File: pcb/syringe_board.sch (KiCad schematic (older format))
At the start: 33 parts, among them J1 PJ-037A, J2 0855025008, J3 OSTVN08A150, J4 10118194-0001LF, U1 TMC2130, U2 ROF-78E3.3-0.5SMD-R, U3 ATMEGA32U4, X1 feather_wing, Y1 8MHz

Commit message: pcb v3.1
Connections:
- net A2 is gone; now on net CS: U3.38 (PF5(ADC5)), X1.7 (A2)
- net A3 is gone; now on net LIMIT1: U3.39 (PF4(ADC4)), X1.8 (A3)
- net 12VDC: now also C3.1; no longer C3.2
- net 3.3VDC: now also R5.1, R6.1
- net CS: no longer U3.8 (PB0(SS))
- net GND: now also C3.2, U1.2 (CLK); no longer C3.1, R5.1, R6.1
- net LIMIT1: no longer U3.37 (PF6(ADC6)), X1.6 (A1)
- net SCL: now also R6.2, X1.18 (SCL)
- net SDA: now also R5.2, X1.17 (SDA)
- new net A1: U3.37 (PF6(ADC6)), X1.6 (A1)
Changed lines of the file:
@@
 Sheet 1 1
 Title "Syringe Board"
-Date "2019-06-12"
-Rev "3.0"
+Date "2019-06-19"
+Rev "3.1"
 Comp "Andy Lustig"
 Comment1 ""
@@
 $EndComp
 Wire Wire Line
-	3300 2000 3100 2000
-Wire Wire Line
 	2700 1800 2700 1700
-Wire Wire Line
-	2700 1700 3100 1700
 Text Label 3400 1700 2    50   ~ 0
 GND
@@
 Wire Wire Line
 	7400 5700 7300 5700
-Text Label 7400 5650 0    50   ~ 0
-GND
 $Comp
 L Device:LED D1
@@
 Text Label 7600 2500 2    50   ~ 0
 MTR_ENABLE
-Text Label 7600 2600 2    50   ~ 0
-LIMIT1
-Text Label 7600 2700 2    50   ~ 0
-A2
-Text Label 7600 2800 2    50   ~ 0
-A3
 $Comp
 L asl_symbols:feather_wing X1
@@
 Wire Wire Line
 	5550 5400 5450 5400
-Text Label 5450 4300 2    50   ~ 0
-A2
-Text Label 5450 4400 2    50   ~ 0
-A3
 Wire Wire Line
 	7600 3400 7700 3400
@@
 Text Label 5450 4100 2    50   ~ 0
 MTR_ENABLE
-Text Label 5450 4200 2    50   ~ 0
-LIMIT1
 Wire Wire Line
 	7700 3900 7650 3900
@@
 GND
 Wire Wire Line
-	7700 4800 7600 4800
-Text Label 7600 4800 2    50   ~ 0
-CS
-Wire Wire Line
 	1950 4100 1850 4100
 Text Label 1850 4100 2    50   ~ 0
@@
 F 3 "~" H 3100 1850 50  0001 C CNN
 	1    3100 1850
-	1    0    0    -1
-$EndComp
-Wire Wire Line
-	3100 1750 3100 1700
-Connection ~ 3100 1700
-Wire Wire Line
-	3100 1700 3700 1700
-Wire Wire Line
-	3100 1950 3100 2000
-Connection ~ 3100 2000
-Wire Wire Line
-	3100 2000 2700 2000
+	1    0    0    1
+$EndComp
 Text Label 9200 3800 2    50   ~ 0
 D+
@@
 	1    0    0    -1
 $EndComp
+Wire Wire Line
+	2700 1700 3100 1700
+Wire Wire Line
+	2700 2000 3100 2000
+Wire Wire Line
+	3100 1750 3100 1700
+Connection ~ 3100 1700
+Wire Wire Line
+	3100 1700 3700 1700
+Wire Wire Line
+	3100 1950 3100 2000
+Connection ~ 3100 2000
+Wire Wire Line
+	3100 2000 3300 2000
+Text Label 7400 5650 0    50   ~ 0
+3.3VDC
+Text Label 6950 5600 0    50   ~ 0
+SDA
+Text Label 6950 5700 0    50   ~ 0
+SCL
+Wire Wire Line
+	1950 4000 1850 4000
+Text Label 1850 4000 2    50   ~ 0
+GND
+Text Label 7600 2800 2    50   ~ 0
+LIMIT1
+Text Label 7600 2700 2    50   ~ 0
+CS
+Text Label 7600 2600 2    50   ~ 0
+A1
+Text Label 5450 4400 2    50   ~ 0
+LIMIT1
+Text Label 5450 4300 2    50   ~ 0
+CS
+Text Label 5450 4200 2    50   ~ 0
+A1
 $EndSCHEMATC

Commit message: pcb rev 3.2
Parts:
- removed C8: 470nF, Capacitor_SMD:C_0603_1608Metric, symbol Device:C_Small
- removed R3: 2.2Ω, Resistor_SMD:R_0603_1608Metric, symbol Device:R_Small_US
- removed U1: TMC2130, Package_QFP:TQFP-48-1EP_7x7mm_P0.5mm_EP5x5mm_ThermalVias, symbol asl_symbols:TMC2130
- added U1: TMC2208, Package_DFN_QFN:QFN-28-1EP_5x5mm_P0.5mm_EP3.35x3.35mm_ThermalVias, symbol asl_symbols:TMC2208
- C6: renamed from C7; value 4.7uF -> 2.2µF
- renumbered C2 to C1, C6 to C2, C4 to C3, C1 to C4, C3 to C7, R4 to R3, R5 to R4, R6 to R5, R7 to R6, R8 to R7
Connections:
- net 12VDC: now also C2.1, C3.2, C4.1, U1.22 (VS), U1.28 (VS)
- net 3.3VDC: now also C5.2, U1.15 (VCC_IO)
- net D6: now also U1.14 (PDN_UART)
- net DIR: now also U1.19 (DIR)
- net GND: now also C2.2, C5.1, R1.1, U1.13 (CLK), U1.18 (GND), U1.29 (DIE_PAD), U1.3 (GND); no longer C2.1, C4.2, C5.2, R1.2
- net MTR_ENABLE: now also U1.2 (ENN)
- net STEP: now also U1.16 (STEP)
- net at J3.1 (Pin_1): now also U1.24 (OA1)
- net at J3.2 (Pin_2): now also U1.21 (OA2)
- net at J3.3 (Pin_3): now also U1.26 (OB1)
- net at J3.4 (Pin_4): now also U1.1 (OB2)
- net at R2.1: now also U1.23 (BRA)
- net at C6.2: now also U1.8 (5VOUT)
- net at C1.2: now also U1.5 (CPI)
- net at C1.1: now also U1.4 (CPO)
- new net: C4.2, U1.6 (VCP)
- new net: R1.2, U1.27 (BRB)
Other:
- moved on the sheet: C1, C2, C3, C4, C5, C6, J3, R1, R2

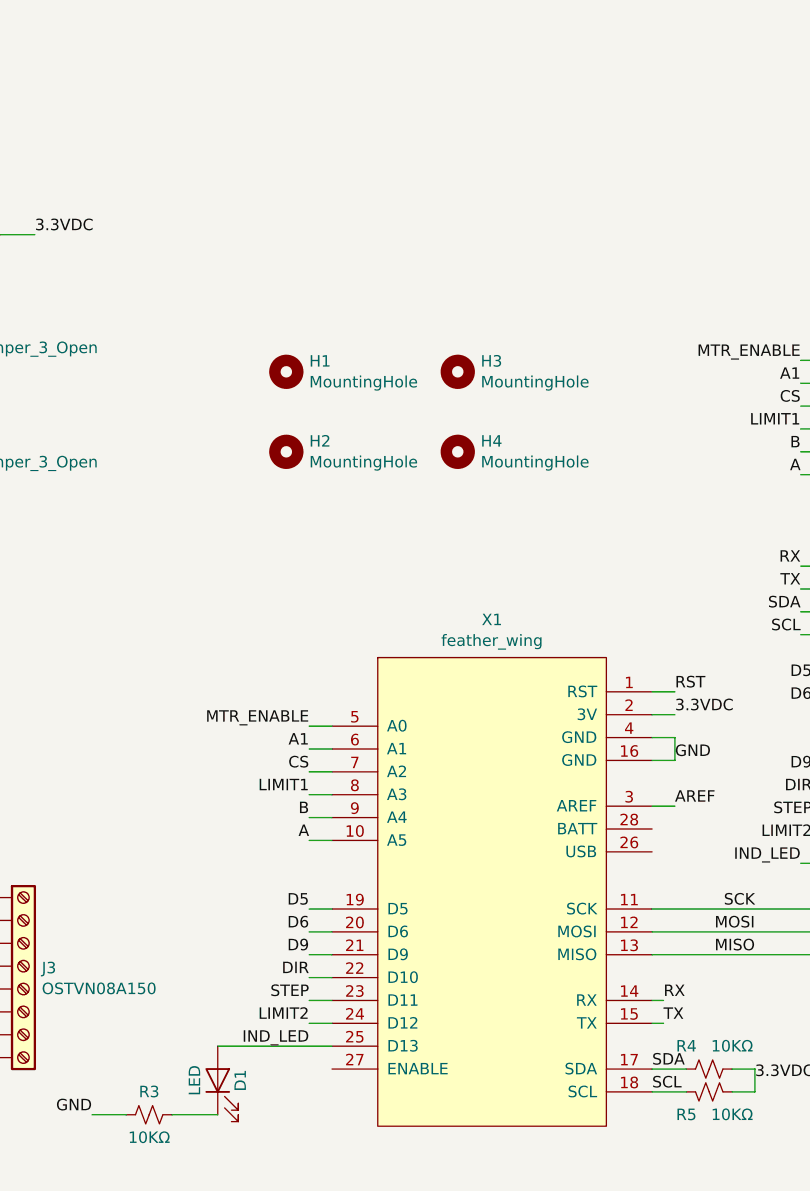
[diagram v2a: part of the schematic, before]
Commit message: PCB updates. Added BOM info. enlarged mounting holes. added footprints for female headers
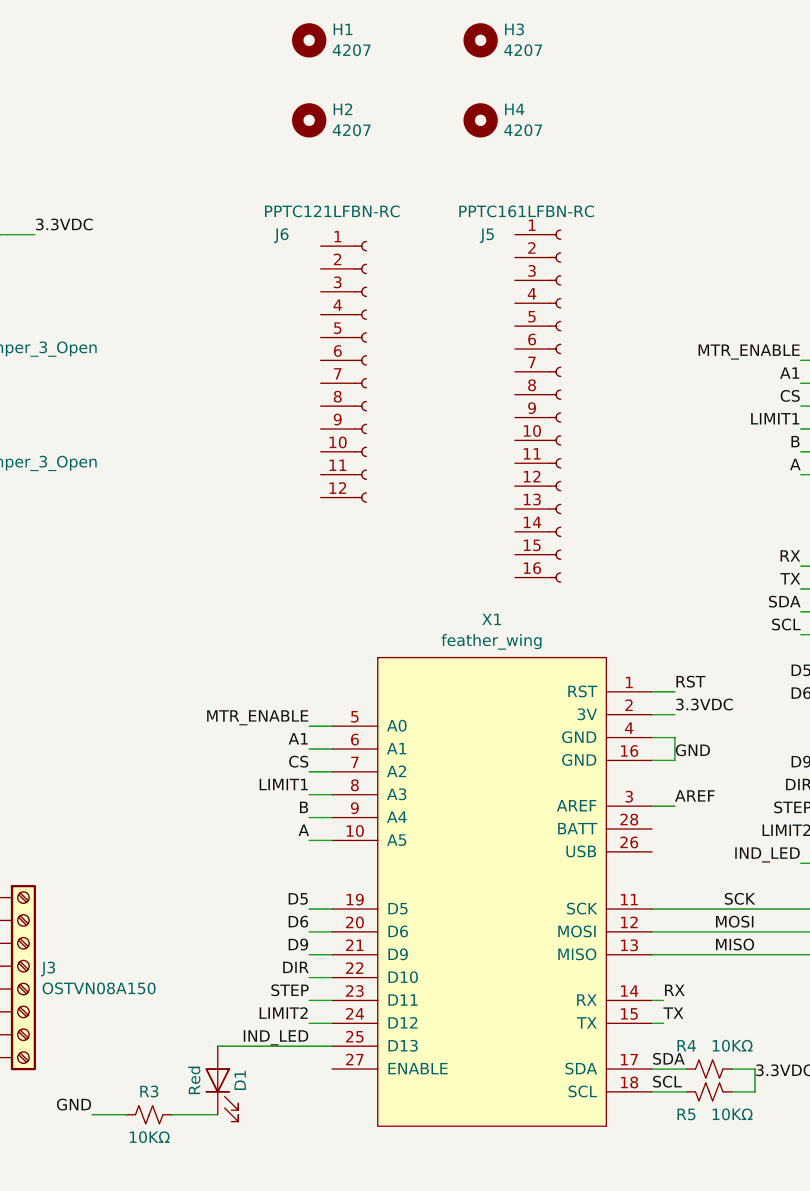
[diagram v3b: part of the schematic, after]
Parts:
- added J5: PPTC161LFBN-RC, Connector_PinSocket_2.54mm:PinSocket_1x16_P2.54mm_Vertical, symbol Connector:Conn_01x16_Female
- added J6: PPTC121LFBN-RC, Connector_PinSocket_2.54mm:PinSocket_1x12_P2.54mm_Vertical, symbol Connector:Conn_01x12_Female
- C7: Description (none) -> Electrolytic Capacitor
- D1: value LED -> Red; Description (none) -> Indicator LED
- H1, H2, H3, H4: value MountingHole -> 4207; Description (none) -> Standoff
- J1: Description (none) -> DC Jack
- J2: Description (none) -> RJ45 Jack
- J3: Description (none) -> 8pos Screw Terminal
- J4: Description (none) -> Micro USB Socket
- JP1, JP2, X1: DNP (none) -> 1
- S1: Description (none) -> Tactile switch
- U1: Description (none) -> Motor Driver IC
- U2: Description (none) -> 3.3V Voltage Regulator
- U3: Description (none) -> Microcontroller
- Y1: Description (none) -> Resonator
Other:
- moved on the sheet: H1, H2, H3, H4
